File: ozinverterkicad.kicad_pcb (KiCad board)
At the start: 2 copper layers, 169.4 x 86 mm, 68 parts, among them P1 topowerboard, P2 PwrLED, P3 on/off, P4 temp, P5 ct sense, P6 Active mains, P7 neutral mains, P8 systemled, Q1 tip35c, Q2 tip35c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

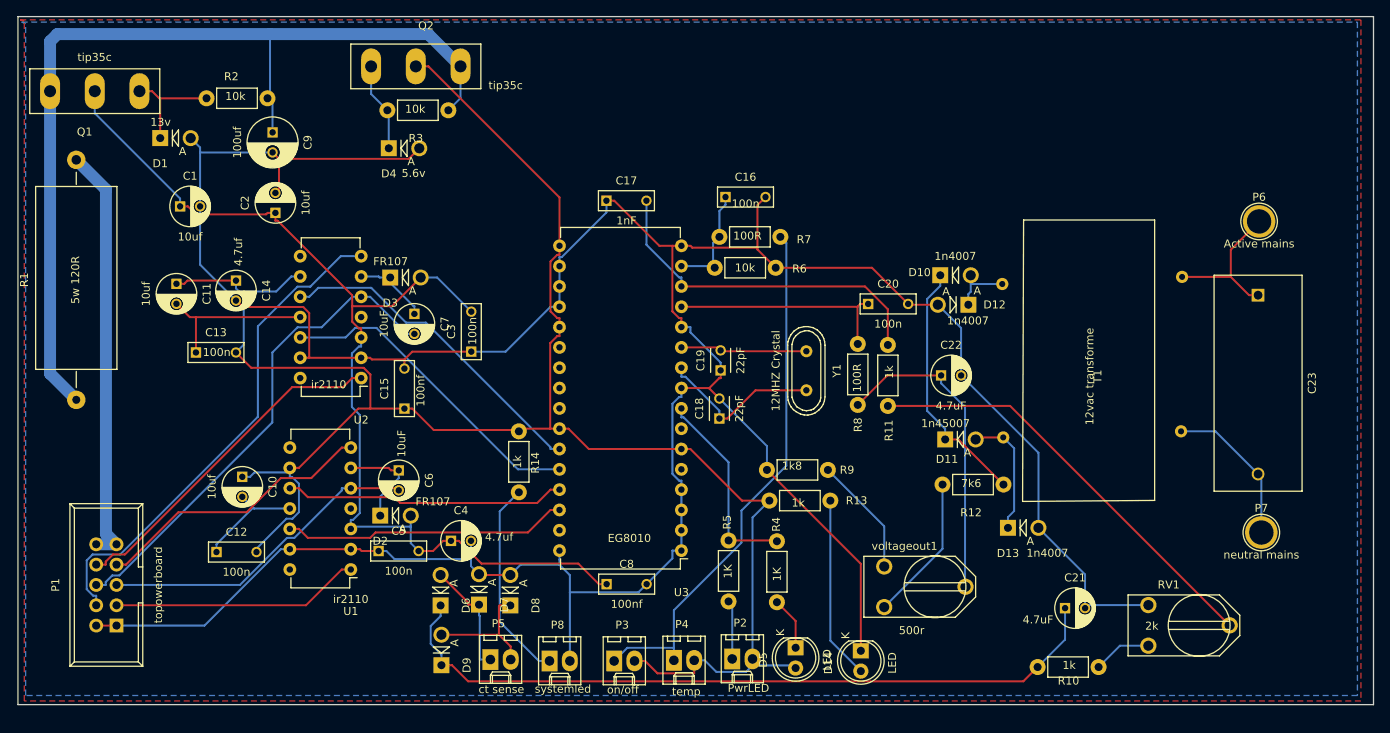
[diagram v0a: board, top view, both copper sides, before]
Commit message: reworked with connector changes
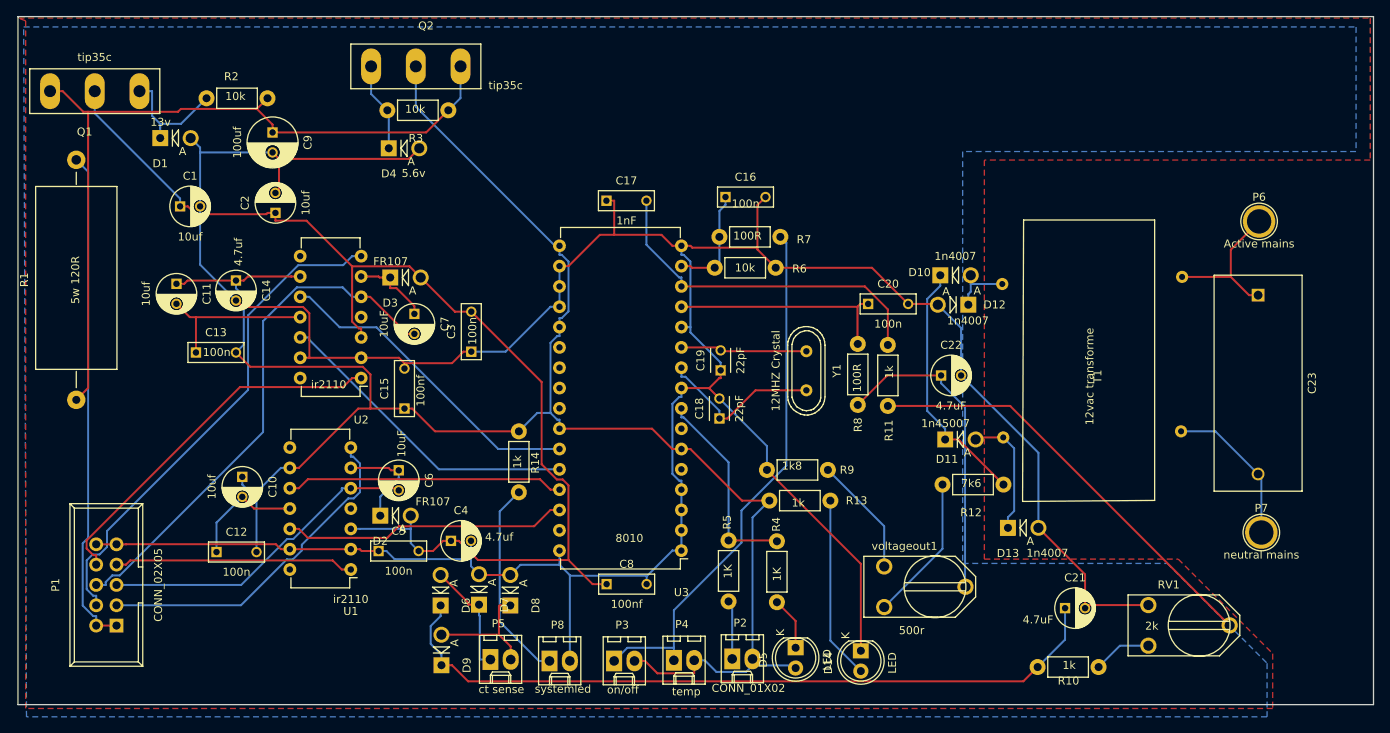
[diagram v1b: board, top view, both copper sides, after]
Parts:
- P1: value topowerboard -> CONN_02X05
- P2: value PwrLED -> CONN_01X02
- U3: value EG8010 -> 8010
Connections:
- P1 pad 1: GND -> +48V
- P1 pad 10: +48V -> GND
- P1 pad 2: GND -> +48V
- P1 pad 9: +48V -> GND
- U1 pad 1: Net-(P1-Pad3) -> Net-(P1-Pad7)
- U1 pad 7: Net-(P1-Pad7) -> Net-(P1-Pad3)
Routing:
- net /24vin: track 118.4 -> 98.6 mm
- net +12V: track 133.9 -> 146.0 mm
- net Net-(P1-Pad3): track 31.1 -> 42.9 mm
- net +48V: track 52.7 -> 62.6 mm
- net Net-(P1-Pad7): track 35.3 -> 30.0 mm
- net Net-(C7-Pad2): track 62.0 -> 65.9 mm
- net GND: track 415.2 -> 411.2 mm
- net +5V: track 236.3 -> 232.5 mm
- net Net-(P1-Pad8): track 43.0 -> 46.5 mm
- net Net-(D1-Pad1): track 13.7 -> 15.0 mm
- net Net-(U2-Pad10): track 41.4 -> 40.3 mm
- net Net-(U2-Pad12): track 40.2 -> 39.4 mm
- net Net-(C10-Pad2): track 14.0 -> 14.8 mm
